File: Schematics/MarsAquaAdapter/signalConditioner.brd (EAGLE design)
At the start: 50.8 x 32.7 mm, 19 parts, among them IC3 LMV358SOIC, Q2 MMBT4403

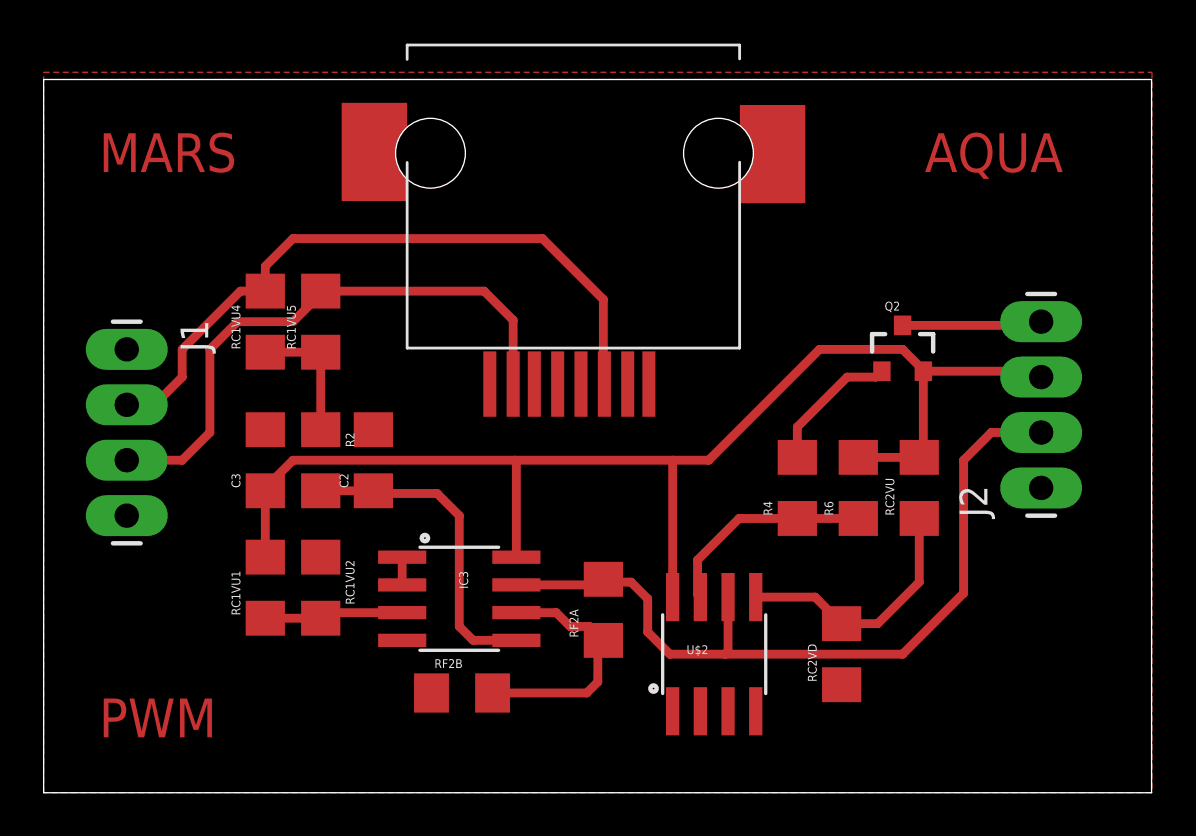
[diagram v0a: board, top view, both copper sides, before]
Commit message: Add pull down and update divider
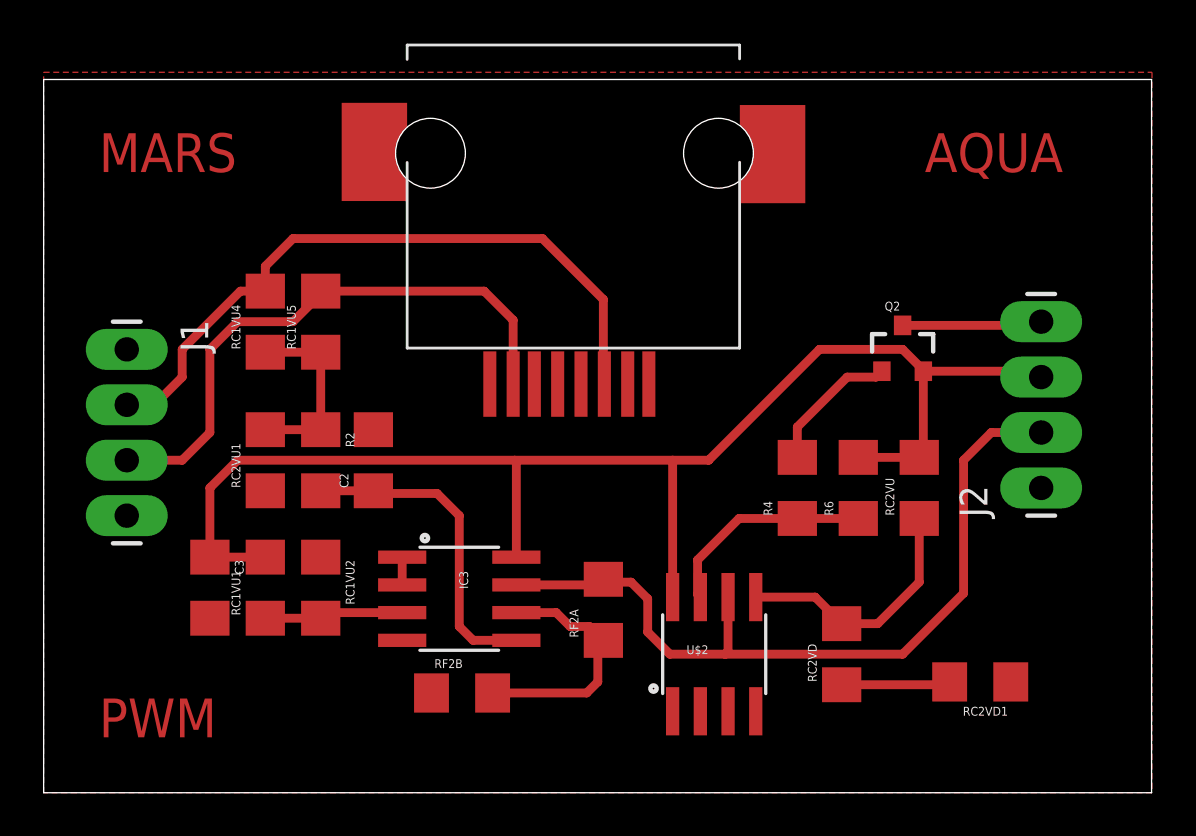
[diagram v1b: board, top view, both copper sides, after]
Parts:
- added RC2VD1: 4.7k, SparkFun-Resistors:1206
- added RC2VU1: 330k, SparkFun-Resistors:1206
- RC2VD: value 18k -> 20k
- moved C3 6.37 mm to (7.62, 9.40), turned to 270 degrees
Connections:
- new net N$2: RC2VD.1, RC2VD1.2
- net GND: now also RC2VD1.1, RC2VU1.1; no longer RC2VD.1
- net INPUT: now also RC2VU1.2
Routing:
- net 12V: track 59.5 -> 64.6 mm
- net N$2: track 0.00 -> 5.08 mm
- net INPUT: track 6.09 -> 8.63 mm
